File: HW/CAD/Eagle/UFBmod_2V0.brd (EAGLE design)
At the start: 78.1 x 89.5 mm, 71 parts, among them U301 MAX5217, U401 AT86RF215-ZU, U411 ASVTX-13-D-26.000MHZ-I05-T, U511 PE4259, U521 RFX1010, U581 B39871B3440U410, X1 TTE_EN11-HSM, X591 ANTENNATINY, X595 ANTENNATINY, X711 MOLEX 105017-0001, X721 PHOENIX_1990067_1X8X2MM50_PTS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, X722 PHOENIX_1990067_1X8X2MM50_PTS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, X723 PHOENIX_1990067_1X8X2MM50_PTS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

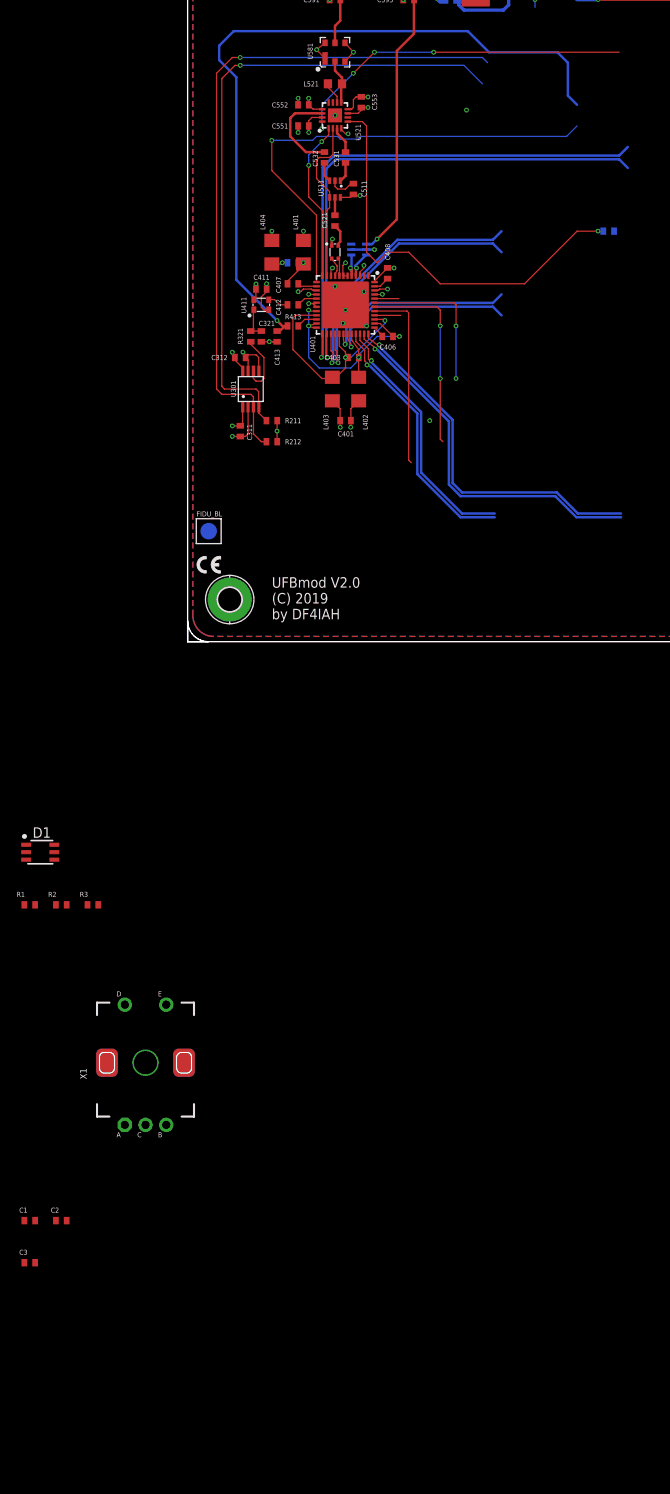
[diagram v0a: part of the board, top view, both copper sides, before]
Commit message: HW_2V0 - HW/CAD/Eagle - RFX1010 application schematic adapted
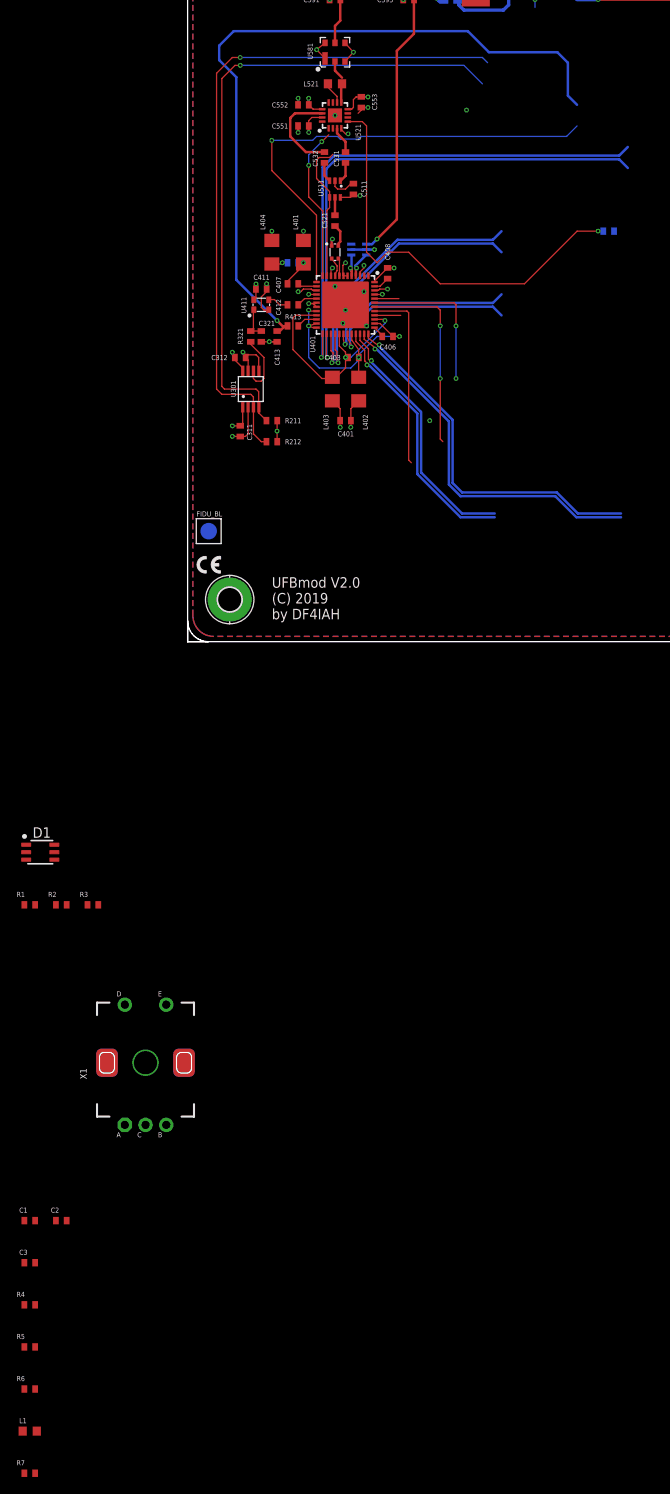
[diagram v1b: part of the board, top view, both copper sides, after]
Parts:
- added L1: 6.8nH, df4iah_rcl:L0603
- added R4, R5, R6, R7: 10kR, df4iah_rcl:R0402
- C551, C552, C553: value 100nF -> 10nF
- L521: value ? nH -> 2.7nH
- R521: value 1kR -> 100R
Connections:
- net FE09_IND renamed RFX_IND
- net FPGA_FE09_DET renamed FPGA_RFX_DET
- removed net FE09_DET: R521.1, U521.5
- removed net FE09_MODE: U521.16
- new net FPGA_RFX_MODE: R7.1
- new net RFX_DET: R521.1, R6.2, U521.5
- new net RFX_MODE: R7.2, U521.16
- new net RFX_RXEN: R4.2, U521.1
- new net RFX_TXEN: R5.2, U521.2
- new net RFX_VDD3: L1.2, U521.7
- net +3V3: now also L1.1; no longer U521.7
- net FE09_ANT: no longer L521.2
- net GND: now also L521.2, R6.1
- net TRX_FEA09: now also R5.1; no longer U521.2
- net TRX_FEB09: now also R4.1; no longer U521.1
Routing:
- net RFX_DET: track 0.00 -> 51.5 mm, vias 0 -> 1
- net FE09_DET: track 51.5 -> 0.00 mm, vias 1 -> 0
- net FE09_MODE: track 42.2 -> 0.00 mm, vias 4 -> 0
- net TRX_FEA09: track 20.2 -> 17.0 mm
- net +3V3: track 36.0 -> 34.8 mm
- net FE09_ANT: track 5.34 -> 4.46 mm
- net TRX_FEB09: track 19.5 -> 18.7 mm

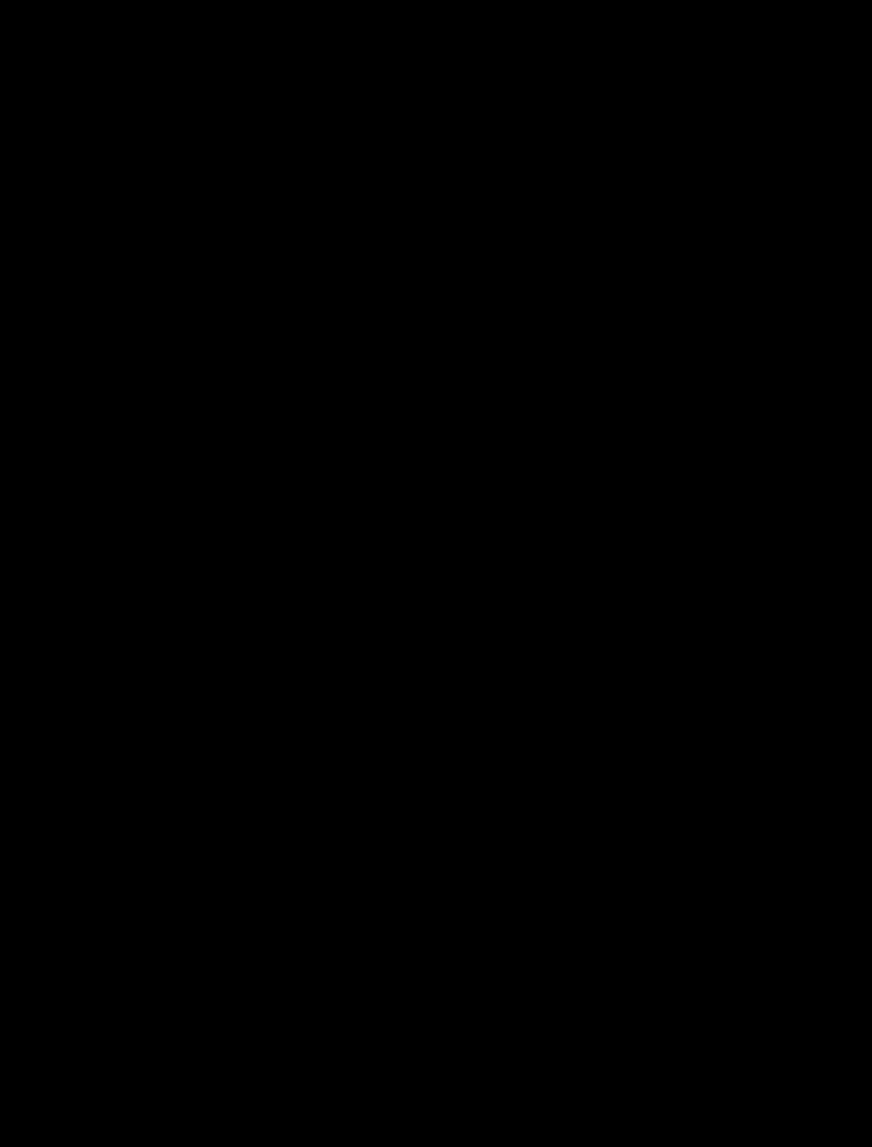
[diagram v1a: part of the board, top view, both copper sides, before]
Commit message: HW_2V0 - HW/CAD/Eagle/lbr - df4iah_connector.lbr SEMTEC LSHM-150-02.5-L-DV-A-S-K-TR and LSHM-130-02.5-L-DV-A-S-K-TR added
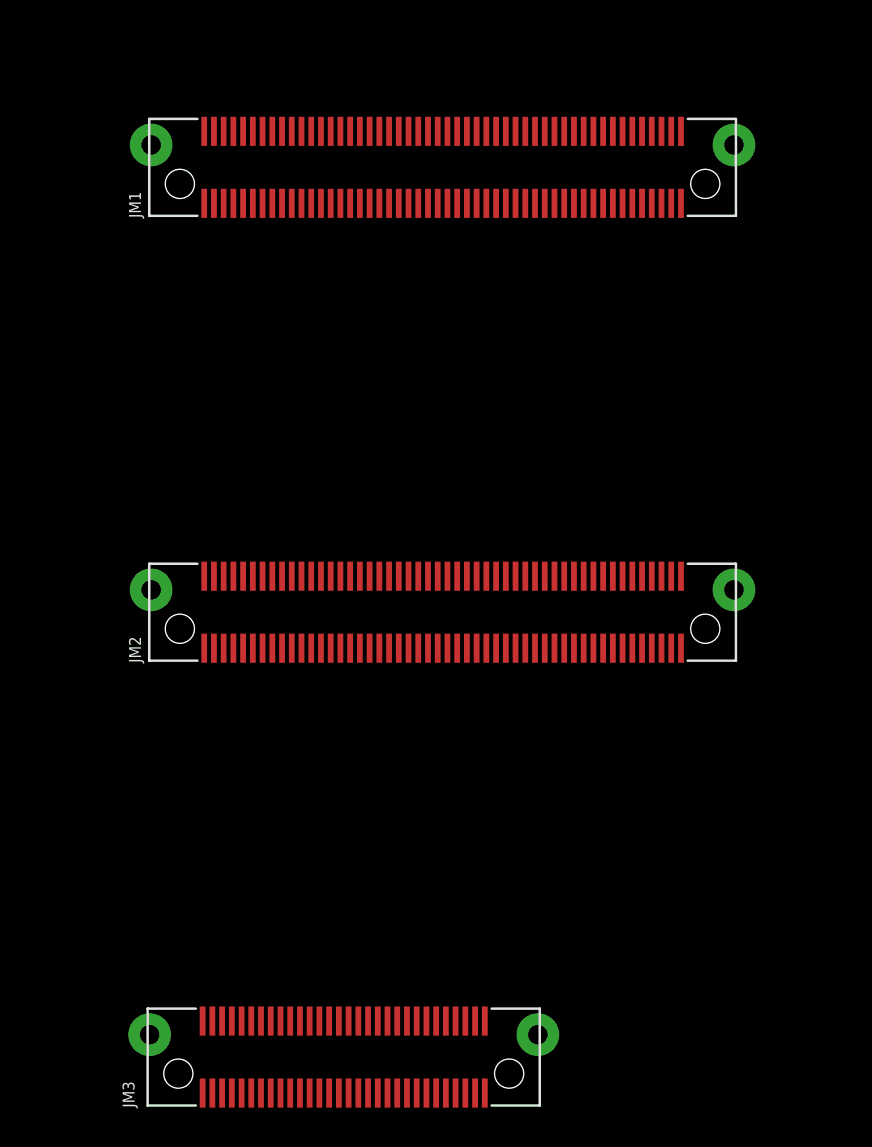
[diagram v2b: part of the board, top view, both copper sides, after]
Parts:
- added JM1, JM2: LSHM-150-02.5-L-DV-A-S-K-TR, df4iah_connector:SAMTEC_LSHM-150-DV
- added JM3: LSHM-130-02.5-L-DV-A-S-K-TR, df4iah_connector:SAMTEC_LSHM-130-DV
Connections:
- net GND: now also JM1.F1, JM1.F2
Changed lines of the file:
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@@
 <element name="L1" library="df4iah_rcl" package="L0603" value="6.8nH" x="-19.05" y="-95.25"/>
 <element name="R7" library="df4iah_rcl" package="R0402" value="10kR" x="-19.05" y="-100.33"/>
+<element name="JM1" library="df4iah_connector" package="SAMTEC_LSHM-150-DV" value="LSHM-150-02.5-L-DV-A-S-K-TR" x="5.08" y="-115.57"/>
+<element name="JM2" library="df4iah_connector" package="SAMTEC_LSHM-150-DV" value="LSHM-150-02.5-L-DV-A-S-K-TR" x="5.08" y="-138.43"/>
+<element name="JM3" library="df4iah_connector" package="SAMTEC_LSHM-130-DV" value="LSHM-130-02.5-L-DV-A-S-K-TR" x="0" y="-161.29"/>
 </elements>
 <signals>
@@
 <contactref element="R6" pad="1"/>
 <contactref element="L521" pad="2"/>
+<contactref element="JM1" pad="F2"/>
+<contactref element="JM1" pad="F1"/>
 <wire x1="44.45" y1="83.76" x2="73.025" y2="84.455" width="0" layer="19" extent="1-1"/>
 <wire x1="43.33875" y1="83.185" x2="43.18" y2="82.55" width="0" layer="19" extent="1-1"/>
@@
 <wire x1="-18.4" y1="-74.93" x2="-18.4" y2="-69.85" width="0" layer="19" extent="1-1"/>
 <wire x1="-19.7" y1="-90.17" x2="-18.4" y2="-74.93" width="0" layer="19" extent="1-1"/>
+<wire x1="-9.895" y1="-113.57" x2="-19.7" y2="-90.17" width="0" layer="19" extent="1-1"/>
+<wire x1="20.055" y1="-113.57" x2="-9.895" y2="-113.57" width="0" layer="19" extent="1-1"/>
 <wire x1="73.025" y1="5.08" x2="29.21" y2="26.67" width="0" layer="19" extent="1-1"/>
 </signal>

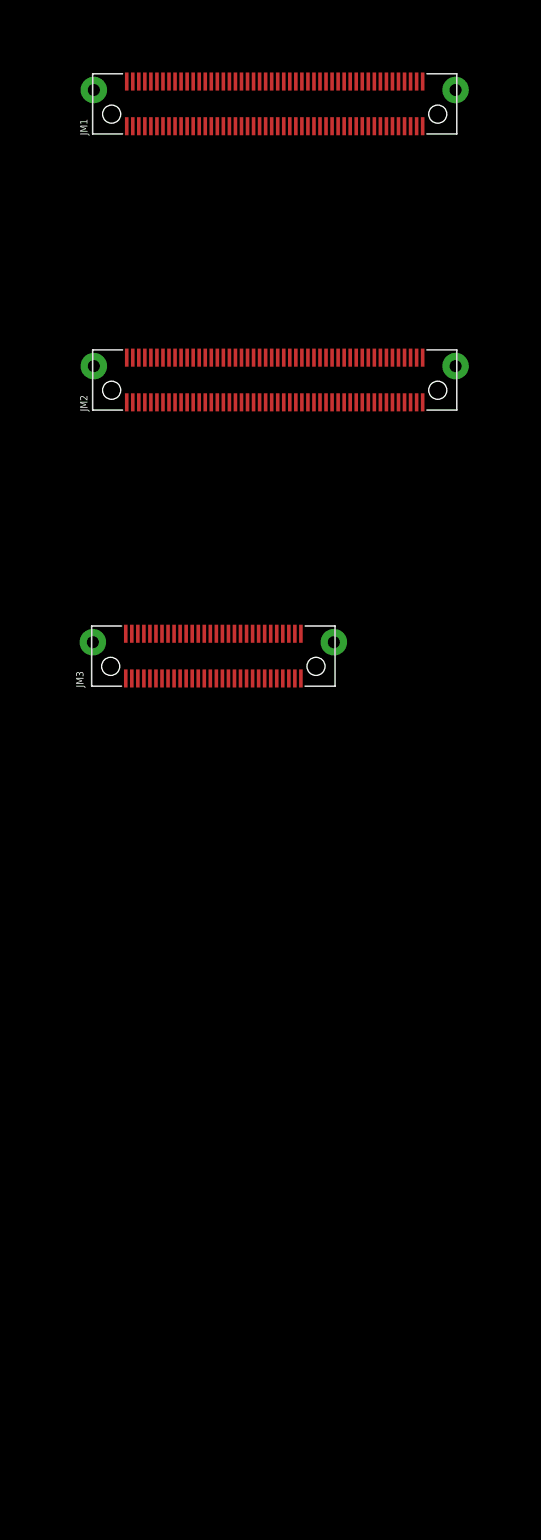
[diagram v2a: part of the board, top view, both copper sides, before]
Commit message: HW_2V0 - HW/CAD/Eagle/lbr - df4iah_connector.lbr SEMTEC LSHM-150-02.5-L-DV-A-S-K-TR and LSHM-130-02.5-L-DV-A-S-K-TR fixed
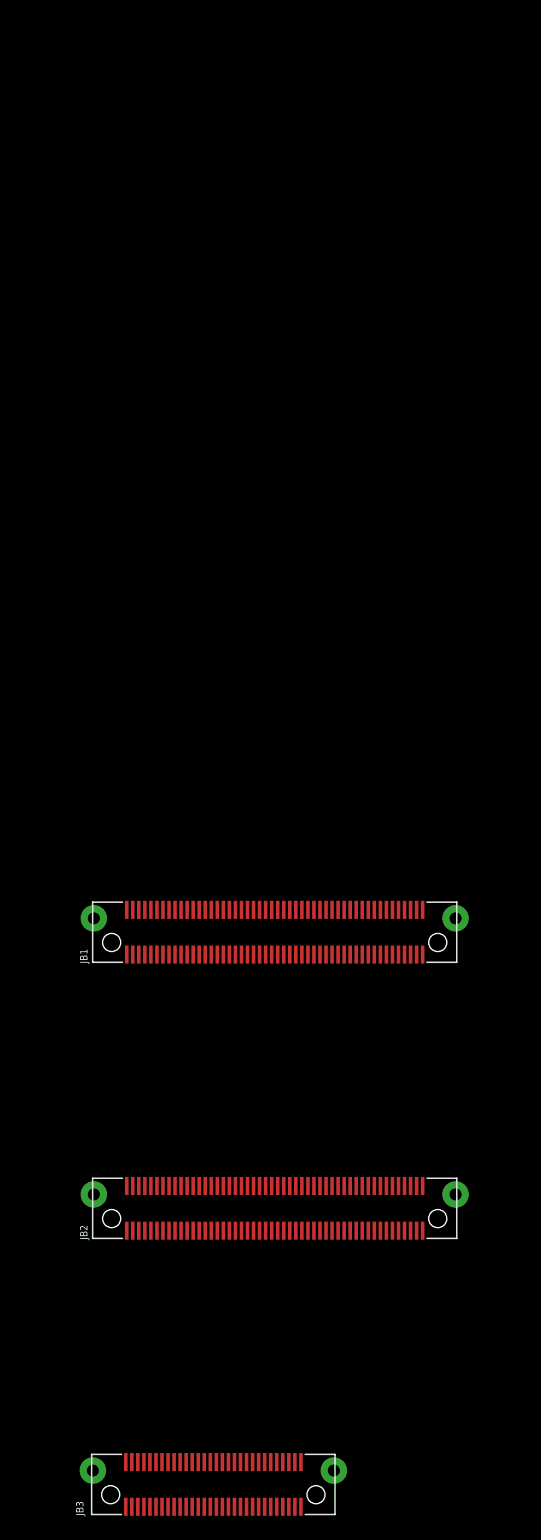
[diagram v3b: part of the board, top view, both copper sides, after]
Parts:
- removed JM1, JM2: LSHM-150-02.5-L-DV-A-S-K-TR, df4iah_connector:SAMTEC_LSHM-150-DV
- removed JM3: LSHM-130-02.5-L-DV-A-S-K-TR, df4iah_connector:SAMTEC_LSHM-130-DV
- added JB1, JB2: (no value), df4iah_connector:SAMTEC_LSHM-150-DV
- added JB3: (no value), df4iah_connector:SAMTEC_LSHM-130-DV
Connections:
- new net U3V3IN: JB1.14, JB1.16
- new net VBAT_IN: JB1.80
- new net VCCIO13: JB2.2, JB2.4
- new net VCCIO15: JB2.10, JB2.8
- new net VCCIO16: JB1.10, JB1.12
- new net VIN: JB1.2, JB1.4, JB1.6, JB2.1, JB2.3, JB2.5, JB2.7
- net GND: now also JB1.F1, JB1.F2, JB2.F1, JB2.F2, JB3.F1, JB3.F2; no longer JM1.F1, JM1.F2

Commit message: HW_2V0 - HW/CAD/Eagle - board size changed
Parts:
- removed C601: 10uF, df4iah_rcl:C0603
- removed C621: 22uF, df4iah_rcl:C0603
- removed C711: 1nF, df4iah_rcl:C0402
- removed H2311, H2321, H2331, H2341: MOUNT-PAD-ROUND2.8, df4iah_holes:2,8-PAD
- removed L611: 440nH, df4iah_rcl:L1812
- removed PF711: 1.1A/2.2A, rcl:M1206
- removed R3: 820R, df4iah_rcl:R0402
- removed R521: 100R, df4iah_rcl:R0402
- removed R711: 330kR, df4iah_rcl:R0402
- removed X1: TTE_EN11-HSM, df4iah_switch:TTE_EN11-HSM
- removed X711: MOLEX 105017-0001, df4iah_connector:USB-B-MICRO-SMD_MOLEX-105017-0001
- removed X721, X722, X723: PHOENIX_1990067_1X8X2MM50_PTSA-0-5, df4iah_connector:PHOENIX_1990067_1X8X2MM50_PTSA-0-5
- added C0501: 100nF, df4iah_rcl:C0402
- added C0511, C0512: 1uF, df4iah_rcl:C0402
- added C1121: 22uF, df4iah_rcl:C0603
- added C1211: 1nF, df4iah_rcl:C0402
- added D1111, D1112: CRS08, df4iah_diode:SOD80C
- added H1311, H1312, H1313, H1314, HB_351, HB_352, HB_353, HB_354: MOUNT-PAD-ROUND3.2, df4iah_holes:3,2-PAD
- added L1101: 440nH, df4iah_rcl:L1812
- added PF1211: 1.1A/2.2A, rcl:M1206
- added R0531: 220kR, df4iah_rcl:R0402
- added R0551: 1.5kR, df4iah_rcl:R0402
- added R0552: 2.0kR, df4iah_rcl:R0402
- added R0553: 27R, df4iah_rcl:R0603
- added R0821: 100R, df4iah_rcl:R0402
- added R1023: 820R, df4iah_rcl:R0402
- added R1211: 330kR, df4iah_rcl:R0402
- added T0551: MMBT2222, transistor:SOT23
- added U0501: MIDAS_MCCOG21605B6W-FPTLWI, df4iah_lcd:MIDAS_MCCOG21605B6W-FPTLWI
- added X1011: TTE_EN11-HSM, df4iah_switch:TTE_EN11-HSM
- added X1211: MOLEX 105017-0001, df4iah_connector:USB-B-MICRO-SMD_MOLEX-105017-0001
- added X1221, X1222, X1223: PHOENIX_1990067_1X8X2MM50_PTSA-0-5, df4iah_connector:PHOENIX_1990067_1X8X2MM50_PTSA-0-5
- moved JB3 284.7 mm to (78.2, 43.9), turned to 90 degrees
- moved JB1 249.6 mm to (57.1, 59.9)
- moved JB2 240.7 mm to (57.1, 27.9)
- moved FIDU_BR 29.8 mm to (95.9, 11.1)
- moved FIDU_TR 18.7 mm to (87.2, 87.0)
- moved FIDU_BL 2.22 mm to (2.54, 11.1)
- moved FIDU_TL 1.27 mm to (11.1, 87.0)
- renumbered C1 to C1011, C2 to C1012, C3 to C1013, C311 to C0611, C312 to C0612, C321 to C0621, C401 to C0701, C403 to C0703, C404 to C0704, C406 to C0706, C407 to C0707, C408 to C0708, C411 to C0711, C412 to C0712, C413 to C0713, C511 to C0811, C521 to C0821, C531 to C0831, C532 to C0832, C551 to C0851, C552 to C0852, C553 to C0853, C591 to C0891, C595 to C0895, C597 to C0897, D1 to D1021, L1 to L0853, L401 to L0701, L402 to L0702, L403 to L0703, L404 to L0704, L421 to L0721, L422 to L0722, L521 to L0821, L592 to L0892, L596 to L0896, R1 to R1021, R2 to R1022, R211 to R0411, R212 to R0412, R321 to R0621, R4 to R0862, R413 to R0713, R5 to R0863, R6 to R0822, R7 to R0861, U301 to U0601, U401 to U0701, U411 to U0711, U511 to U0811, U521 to U0821, U581 to U0881, X591 to X0891, X595 to X0895
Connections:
- removed net +5V: C601.1, PF711.1
- new net +5V_USB: D1112.A, PF1211.1
- new net LCD_BL_K: T0551.3, U0501.11
- new net LCD_BL_PWM: R0552.2
- new net LCD_CAP1N: C0511.2
- new net LCD_CAP1P: C0511.1
- new net LCD_NRST: R0531.2
- new net LCD_VOUT: C0512.1
- new net LED_B_B: R0551.2, R0552.1, T0551.1
- new net LED_B_E: R0553.2, T0551.2
- new net VDD: U0501.4
- new net VIN_PWR: D1111.A
- new net VIN_REG: D1111.C, D1112.C
- new net VSS: U0501.5
- net +3V3: now also C0501.1, C1121.1, L1101.1, U0501.12; no longer C621.1, L611.1
- net FPGA_RFX_DET: now also R0821.2; no longer R521.2
- net GND: now also C0501.2, C0512.2, C1121.2, C1211.1, H1311.B3,2, H1312.B3,2, H1313.B3,2, H1314.B3,2, HB_351.B3,2, HB_352.B3,2, HB_353.B3,2, HB_354.B3,2, JB1.1, JB1.19, JB1.25, JB1.30, JB1.33, JB1.43, JB1.53, JB1.54, JB1.63, JB1.64, JB1.7, JB1.73, JB1.74, JB1.83, JB1.89, JB2.19, JB2.29, JB2.39, JB2.40, JB2.49, JB2.50, JB2.59, JB2.60, JB2.69, JB2.70, JB2.79, JB2.80, JB2.89, JB3.11, JB3.17, JB3.18, JB3.23, JB3.24, JB3.29, JB3.30, JB3.35, JB3.36, JB3.45, JB3.46, JB3.5, JB3.6, R0531.1, R0551.1, R0553.1, R1211.1, X1011.C, X1011.D, X1211.GND; no longer C601.2, C621.2, C711.1, H2311.B2,8, H2321.B2,8, H2331.B2,8, H2341.B2,8, R711.1, X1.C, X1.D, X711.GND
- net LED_B1: now also R1023.2; no longer R3.2
- net LED_B_R1: now also R1023.1; no longer R3.1
- net PMIC3V3_SW: now also L1101.2; no longer L611.2
- net RFX_DET: now also R0821.1; no longer R521.1
- net ROT_I_R: now also X1011.A; no longer X1.A
- net ROT_P: now also X1011.E; no longer X1.E
- net ROT_Q_R: now also X1011.B; no longer X1.B
- net USB_SHIELD: now also C1211.2, R1211.2, X1211.JSHIELD, X1211.JSHIELD@2, X1211.JSHIELD@3, X1211.JSHIELD@4, X1211.JSHIELD@5, X1211.JSHIELD@6; no longer C711.2, R711.2, X711.JSHIELD, X711.JSHIELD@2, X711.JSHIELD@3, X711.JSHIELD@4, X711.JSHIELD@5, X711.JSHIELD@6
- net USB_VBUS: now also PF1211.2, X1211.VBUS; no longer PF711.2, X711.VBUS
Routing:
- net FPGA_TRX_CLKO: track 88.6 -> 0.00 mm, vias 1 -> 0
- net FPGA_I2C_SCL: track 83.1 -> 5.21 mm, vias 1 -> 0
- net FPGA_I2C_SDA: track 78.7 -> 2.04 mm, vias 1 -> 0
- net TRX_TXCLK_N: track 64.0 -> 0.00 mm, vias 1 -> 0
- net TRX_TXCLK_P: track 63.2 -> 0.00 mm, vias 1 -> 0
- net TRX_RSTN: track 57.1 -> 0.00 mm, vias 1 -> 0
- net RFX_DET: track 51.5 -> 0.00 mm, vias 1 -> 0
- net TRX_RXD24_N: track 45.2 -> 0.00 mm, vias 1 -> 0
- net TRX_RXD24_P: track 44.5 -> 0.00 mm, vias 1 -> 0
- net +5V: track 42.7 -> 0.00 mm, vias 1 -> 0
- net TRX_TXD_N: track 34.9 -> 0.00 mm, vias 1 -> 0
- net TRX_TXD_P: track 34.2 -> 0.00 mm, vias 1 -> 0
- net TRX_RXCLK_N: track 31.8 -> 0.00 mm, vias 1 -> 0
- net TRX_RXCLK_P: track 31.0 -> 0.00 mm, vias 1 -> 0
- net TRX_SELN: track 24.1 -> 0.00 mm, vias 2 -> 0
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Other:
- board size 78.1 x 89.5 mm -> 98.4 x 89.5 mm
- board text added: "TE0712-02-100-2C3"
